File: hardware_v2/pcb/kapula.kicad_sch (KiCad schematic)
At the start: 166 parts, among them J1 Conn_02x10_Odd_Even, J2 Conn_02x10_Odd_Even, J3 U.FL, J4 U.FL, J5 U.FL, J6 U.FL, Q1 AO3401A, Q1 BSS84, Q2 AO3400A, Q3 AO3400A, Q4 AO3400A, Q5 AO3401A, T1 BW21S7511A01TF, T2 BW21S7511A01TF, T3 BW21S7511A01TF, T4 BW21S7511A01TF, U1 TP4054, U2 DW01+G, U3 XC6206P332MR, U4 FM8002A, U5 EFR32FG14P233F256GM48-B, U6 DSB221SDN, U7 XA213-G4J, Y1 32768 Hz

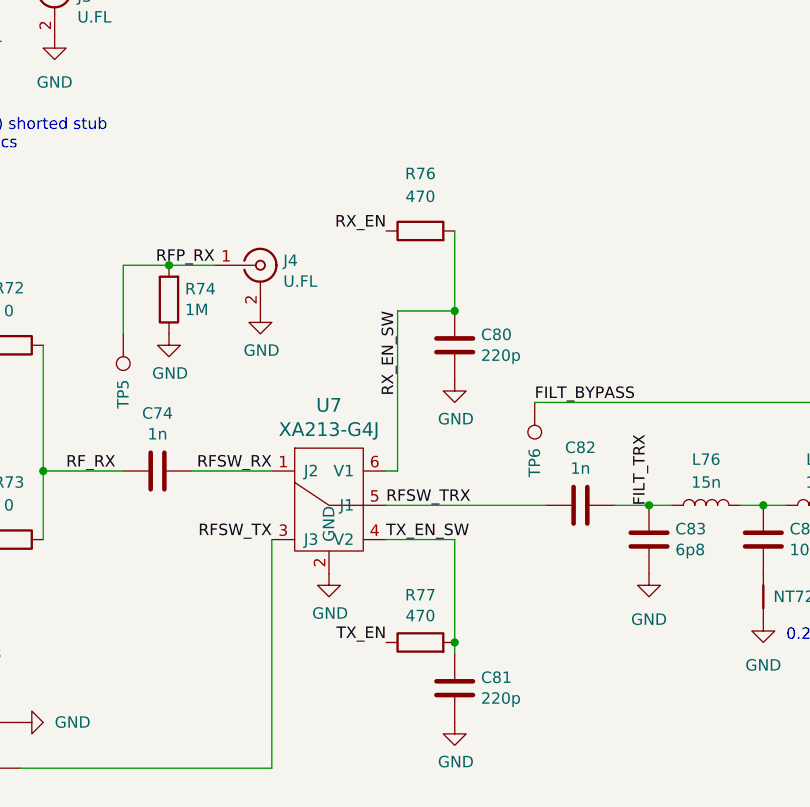
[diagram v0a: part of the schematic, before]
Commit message: PCB: Fix order of RX/TX switch control pins
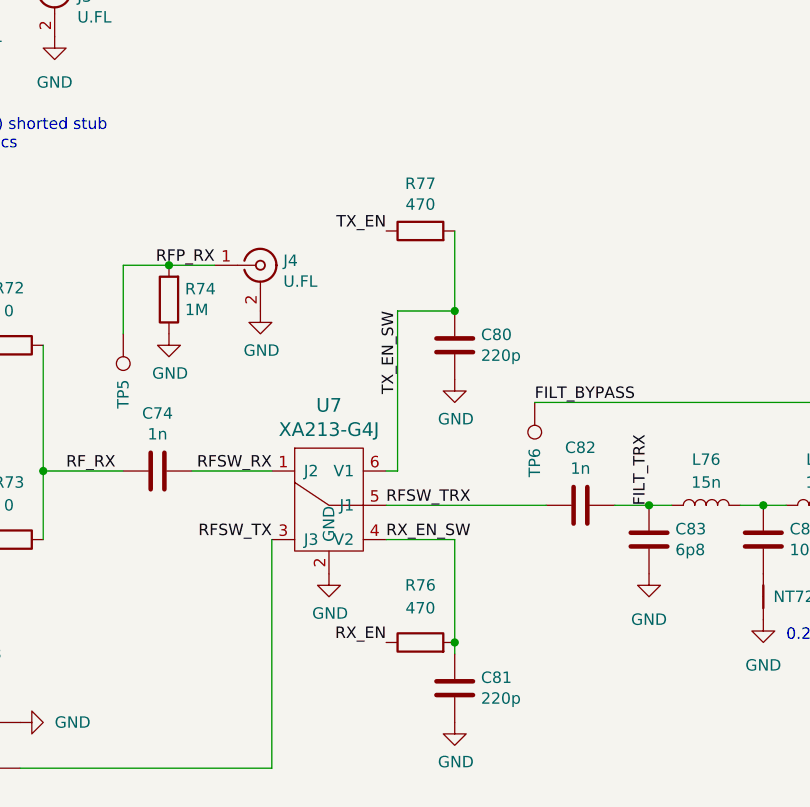
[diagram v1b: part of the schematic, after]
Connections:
- net RX_EN_SW: now also C81.1, U7.4 (V2); no longer C80.1, U7.6 (V1)
- net TX_EN_SW: now also C80.1, U7.6 (V1); no longer C81.1, U7.4 (V2)
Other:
- moved on the sheet: R76, R77
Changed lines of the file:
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@@
   (junction (at 143.51 82.55) (diameter 0) (color 0 0 0 0)
   )
-  (junction (at 283.21 227.33) (diameter 0) (color 0 0 0 0)
-  )
   (junction (at 110.49 238.76) (diameter 0) (color 0 0 0 0)
   )
@@
   (junction (at 200.66 247.65) (diameter 0) (color 0 0 0 0)
   )
+  (junction (at 283.21 227.33) (diameter 0) (color 0 0 0 0)
+  )
   (junction (at 304.8 212.09) (diameter 0) (color 0 0 0 0)
   )
@@
     (stroke (width 0) (type default))
   )
-  (wire (pts (xy 283.21 227.33) (xy 283.21 228.6))
-    (stroke (width 0) (type default))
-  )
   (wire (pts (xy 153.67 82.55) (xy 162.56 82.55))
     (stroke (width 0) (type default))
@@
     (stroke (width 0) (type default))
   )
+  (wire (pts (xy 283.21 227.33) (xy 283.21 228.6))
+    (stroke (width 0) (type default))
+  )
   (wire (pts (xy 53.34 31.75) (xy 44.45 31.75))
     (stroke (width 0) (type default))
@@
     (effects (font (size 1.27 1.27)) (justify left bottom))
   )
-  (label "RX_EN_SW" (at 276.86 190.5 270) (fields_autoplaced)
-    (effects (font (size 1.27 1.27)) (justify right bottom))
+  (label "RX_EN_SW" (at 275.59 215.9 0) (fields_autoplaced)
+    (effects (font (size 1.27 1.27)) (justify left bottom))
   )
   (label "VOL_Out" (at 106.68 102.87 0) (fields_autoplaced)
@@
     (effects (font (size 1.27 1.27)) (justify left bottom))
   )
-  (label "TX_EN_SW" (at 275.59 215.9 0) (fields_autoplaced)
-    (effects (font (size 1.27 1.27)) (justify left bottom))
+  (label "TX_EN_SW" (at 276.86 190.5 270) (fields_autoplaced)
+    (effects (font (size 1.27 1.27)) (justify right bottom))
   )
   (label "D_SDA" (at 364.49 25.4 180) (fields_autoplaced)
@@
     (effects (font (size 1.27 1.27)) (justify right bottom))
   )
-  (label "RX_EN" (at 275.59 181.61 180) (fields_autoplaced)
+  (label "RX_EN" (at 275.59 227.33 180) (fields_autoplaced)
     (effects (font (size 1.27 1.27)) (justify right bottom))
   )
@@
     (effects (font (size 1.27 1.27)) (justify left bottom))
   )
-  (label "TX_EN" (at 275.59 227.33 180) (fields_autoplaced)
+  (label "TX_EN" (at 275.59 181.61 180) (fields_autoplaced)
     (effects (font (size 1.27 1.27)) (justify right bottom))
   )
@@
     )
   )
-  (symbol (lib_id "Device:R") (at 279.4 181.61 90) (unit 1)
+  (symbol (lib_id "Device:R") (at 279.4 227.33 90) (unit 1)
     (in_bom yes) (on_board yes) (dnp no) (fields_autoplaced)
-    (property "Reference" "R76" (at 279.4 175.26 90)
+    (property "Reference" "R76" (at 279.4 220.98 90)
       (effects (font (size 1.27 1.27)))
     )
-    (property "Value" "470" (at 279.4 177.8 90)
+    (property "Value" "470" (at 279.4 223.52 90)
       (effects (font (size 1.27 1.27)))
     )
-    (property "Footprint" "Resistor_SMD:R_0402_1005Metric" (at 279.4 183.388 90)
+    (property "Footprint" "Resistor_SMD:R_0402_1005Metric" (at 279.4 229.108 90)
       (effects (font (size 1.27 1.27)) hide)
     )
-    (property "Datasheet" "" (at 279.4 181.61 0)
+    (property "Datasheet" "" (at 279.4 227.33 0)
       (effects (font (size 1.27 1.27)) hide)
     )
-    (property "LCSC" "C25117" (at 279.4 181.61 0)
+    (property "LCSC" "C25117" (at 279.4 227.33 0)
       (effects (font (size 1.27 1.27)) hide)
     )
@@
     )
   )
-  (symbol (lib_id "Device:R") (at 279.4 227.33 90) (unit 1)
+  (symbol (lib_id "Device:R") (at 279.4 181.61 90) (unit 1)
     (in_bom yes) (on_board yes) (dnp no)
-    (property "Reference" "R77" (at 279.4 222.0722 90)
+    (property "Reference" "R77" (at 279.4 176.3522 90)
       (effects (font (size 1.27 1.27)))
     )
-    (property "Value" "470" (at 279.4 224.3836 90)
+    (property "Value" "470" (at 279.4 178.6636 90)
       (effects (font (size 1.27 1.27)))
     )
-    (property "Footprint" "Resistor_SMD:R_0402_1005Metric" (at 279.4 229.108 90)
+    (property "Footprint" "Resistor_SMD:R_0402_1005Metric" (at 279.4 183.388 90)
       (effects (font (size 1.27 1.27)) hide)
     )
-    (property "Datasheet" "" (at 279.4 227.33 0)
+    (property "Datasheet" "" (at 279.4 181.61 0)
       (effects (font (size 1.27 1.27)) hide)
     )
-    (property "LCSC" "C25117" (at 279.4 227.33 0)
+    (property "LCSC" "C25117" (at 279.4 181.61 0)
       (effects (font (size 1.27 1.27)) hide)
     )

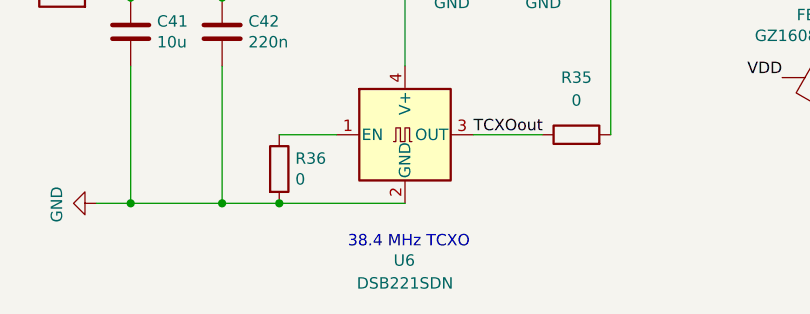
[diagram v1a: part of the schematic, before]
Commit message: PCB: Fix TCXO model in schematic
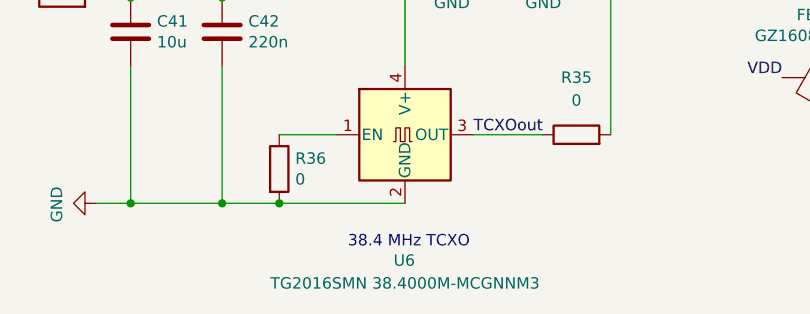
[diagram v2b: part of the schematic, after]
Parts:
- U6: value DSB221SDN -> TG2016SMN 38.4000M-MCGNNM3
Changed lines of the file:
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@@
       (effects (font (size 1.27 1.27)) (justify left))
     )
-    (property "Value" "DSB221SDN" (at 105.41 281.94 0)
+    (property "Value" "TG2016SMN 38.4000M-MCGNNM3" (at 105.41 281.94 0)
       (effects (font (size 1.27 1.27)))
     )

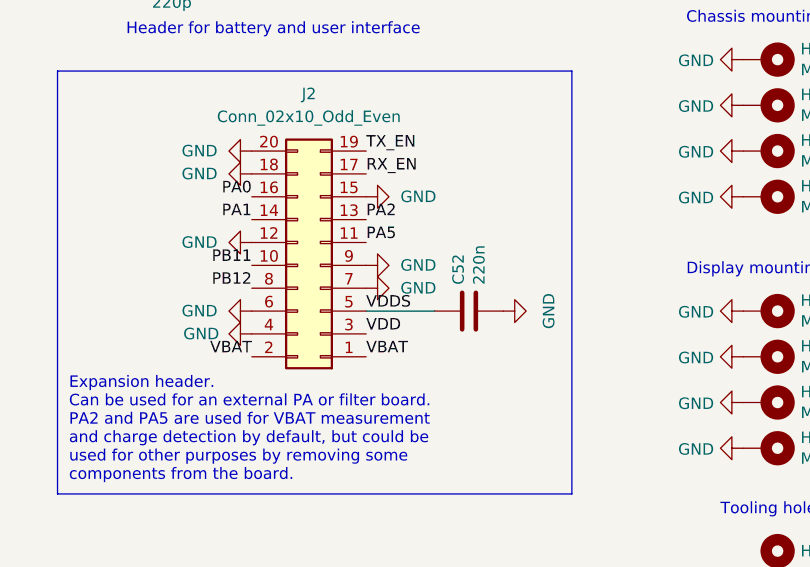
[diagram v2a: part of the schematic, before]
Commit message: PCB: Add DVDD to expansion header
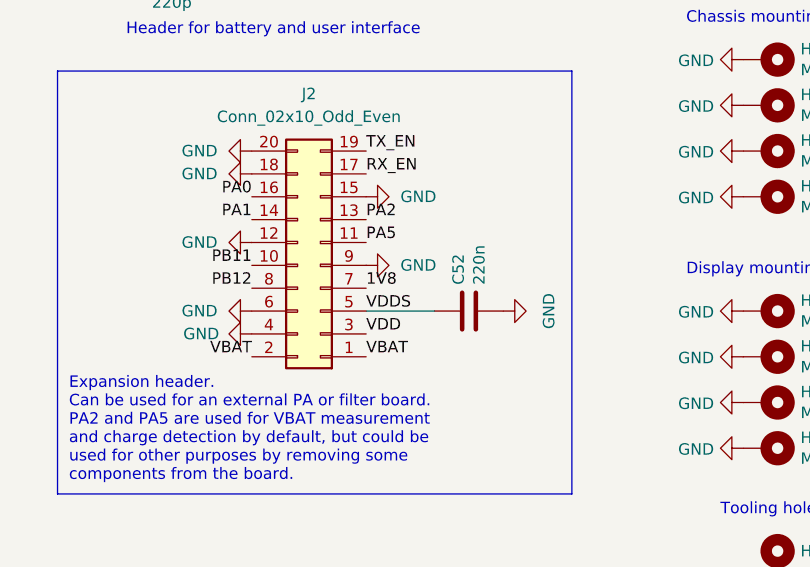
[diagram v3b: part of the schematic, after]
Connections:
- net 1V8: now also J2.7 (Pin_7)
- net GND: no longer J2.7 (Pin_7)
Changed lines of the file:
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@@
     (effects (font (size 1.27 1.27)) (justify right bottom))
   )
+  (label "1V8" (at 344.17 123.19 0) (fields_autoplaced)
+    (effects (font (size 1.27 1.27)) (justify left bottom))
+  )
   (label "VDD" (at 247.65 26.67 0) (fields_autoplaced)
     (effects (font (size 1.27 1.27)) (justify left bottom))
@@
         )
       )
-    )
-  )
-  (symbol (lib_id "power:GND") (at 344.17 123.19 90) (unit 1)
-    (in_bom yes) (on_board yes) (dnp no) (fields_autoplaced)
-    (property "Reference" "#PWR0101" (at 350.52 123.19 0)
-      (effects (font (size 1.27 1.27)) hide)
-    )
-    (property "Value" "GND" (at 347.98 123.19 90)
-      (effects (font (size 1.27 1.27)) (justify right))
-    )
-    (property "Footprint" "" (at 344.17 123.19 0)
-      (effects (font (size 1.27 1.27)) hide)
-    )
-    (property "Datasheet" "" (at 344.17 123.19 0)
-      (effects (font (size 1.27 1.27)) hide)
-    )
-    (pin "1")
-    (instances
-      (project "kapula"
-        (path "/f2315993-072e-45c9-8c85-e79c6d40aba4"
-          (reference "#PWR0101") (unit 1)
-        )
-      )

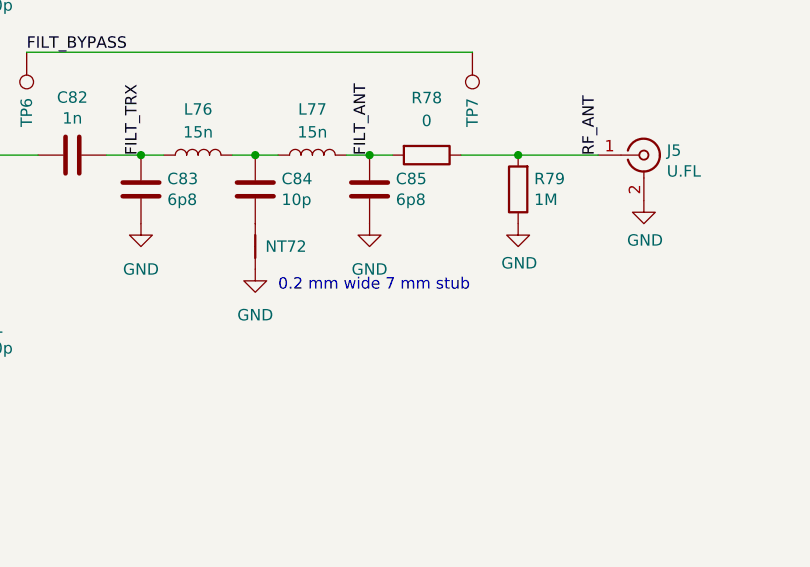
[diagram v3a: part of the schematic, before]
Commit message: PCB: Optimize lowpass filter
* Reduce second harmonic stub length by 1 mm
  to move notch frequency closer to 870 MHz.
* Use footprints of correct size for capacitors and inductors.
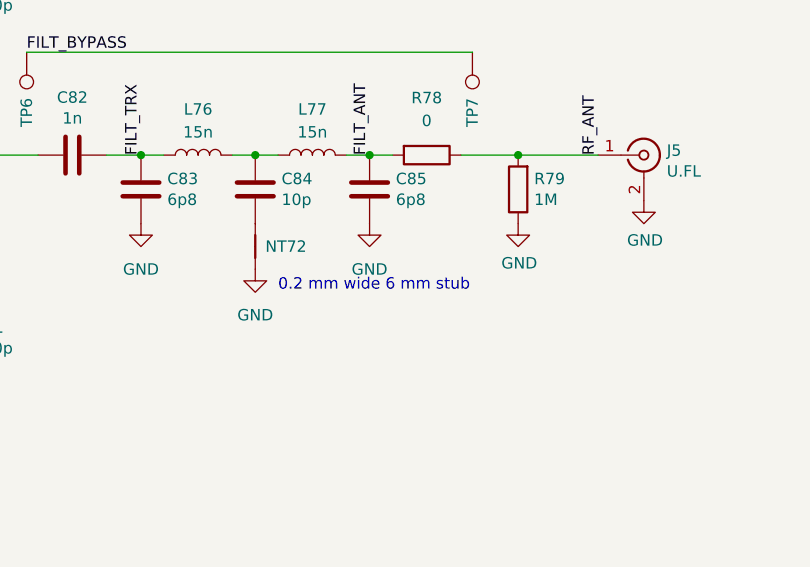
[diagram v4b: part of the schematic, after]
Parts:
- C83, C84, C85: footprint kapula:C_0402_to_0603_HandSolder -> Capacitor_SMD:C_0603_1608Metric_Pad1.08x0.95mm_HandSolder
- L76, L77: footprint kapula:L_0402_to_0603_HandSolder -> Inductor_SMD:L_0402_1005Metric_Pad0.77x0.64mm_HandSolder
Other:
- note added: "0.2 mm wide 6 mm stub"
- note removed: "0.2 mm wide 7 mm stub"
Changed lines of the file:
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@@
     (effects (font (size 1.27 1.27)) (justify left bottom))
   )
-  (text "0.2 mm wide 7 mm stub" (at 320.04 227.33 0)
+  (text "0.2 mm wide 6 mm stub" (at 320.04 227.33 0)
     (effects (font (size 1.27 1.27)) (justify left bottom))
   )
@@
       (effects (font (size 1.27 1.27)) (justify left))
     )
-    (property "Footprint" "kapula:C_0402_to_0603_HandSolder" (at 318.4652 219.71 0)
+    (property "Footprint" "Capacitor_SMD:C_0603_1608Metric_Pad1.08x0.95mm_HandSolder" (at 318.4652 219.71 0)
       (effects (font (size 1.27 1.27)) hide)
     )
@@
       (effects (font (size 1.27 1.27)))
     )
-    (property "Footprint" "kapula:L_0402_to_0603_HandSolder" (at 323.85 212.09 0)
+    (property "Footprint" "Inductor_SMD:L_0402_1005Metric_Pad0.77x0.64mm_HandSolder" (at 323.85 212.09 0)
       (effects (font (size 1.27 1.27)) hide)
     )
@@
       (effects (font (size 1.27 1.27)) (justify left))
     )
-    (property "Footprint" "kapula:C_0402_to_0603_HandSolder" (at 331.1652 219.71 0)
+    (property "Footprint" "Capacitor_SMD:C_0603_1608Metric_Pad1.08x0.95mm_HandSolder" (at 331.1652 219.71 0)
       (effects (font (size 1.27 1.27)) hide)
     )
@@
       (effects (font (size 1.27 1.27)))
     )
-    (property "Footprint" "kapula:L_0402_to_0603_HandSolder" (at 311.15 212.09 0)
+    (property "Footprint" "Inductor_SMD:L_0402_1005Metric_Pad0.77x0.64mm_HandSolder" (at 311.15 212.09 0)
       (effects (font (size 1.27 1.27)) hide)
     )
@@
       (effects (font (size 1.27 1.27)) (justify left))
     )
-    (property "Footprint" "kapula:C_0402_to_0603_HandSolder" (at 305.7652 219.71 0)
+    (property "Footprint" "Capacitor_SMD:C_0603_1608Metric_Pad1.08x0.95mm_HandSolder" (at 305.7652 219.71 0)
       (effects (font (size 1.27 1.27)) hide)
     )

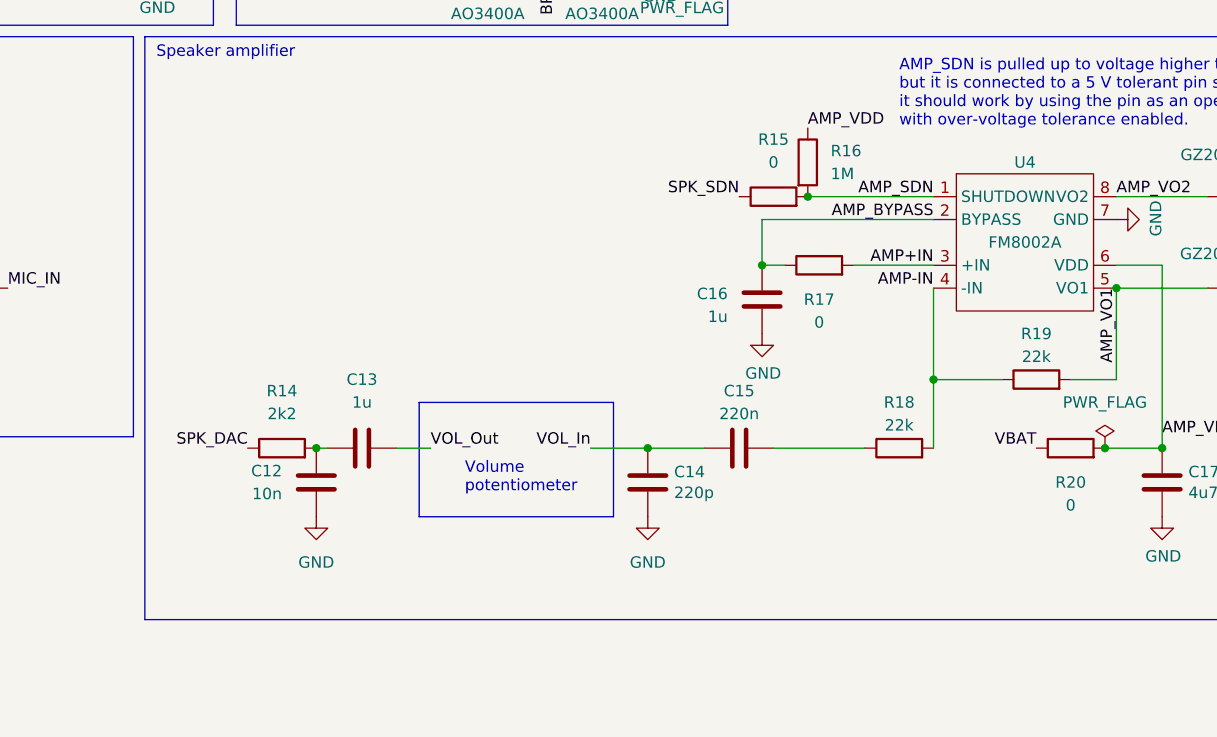
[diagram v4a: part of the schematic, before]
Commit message: PCB: Changes to audio power amplifier circuit
* Increase maximum gain
* Change some footprint sizes
* Reduce shutdown pull-up resistor value
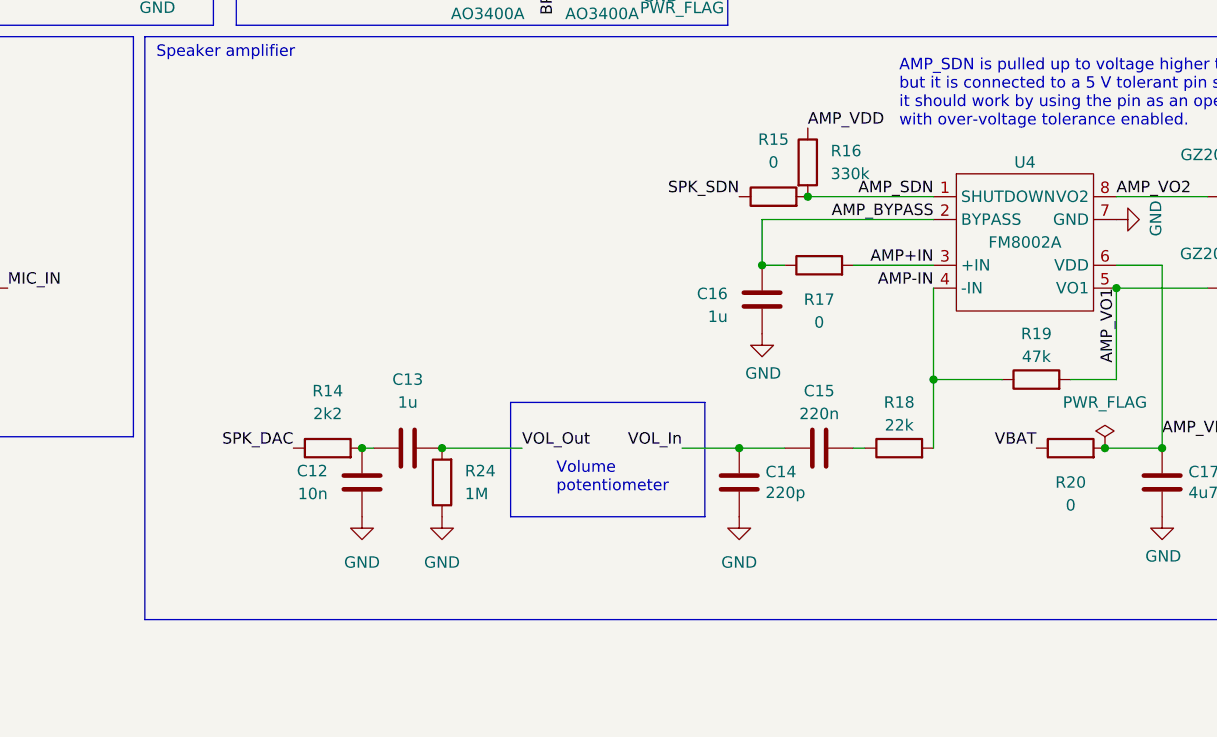
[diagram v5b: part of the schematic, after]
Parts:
- added R24: 1M, Resistor_SMD:R_0402_1005Metric, symbol Device:R
- C15: footprint kapula:C_0402_to_0603_HandSolder -> Capacitor_SMD:C_0402_1005Metric_Pad0.74x0.62mm_HandSolder
- R16: value 1M -> 330k; LCSC C26083 -> C25778
- R18: footprint Resistor_SMD:R_0402_1005Metric -> Resistor_SMD:R_0603_1608Metric_Pad0.98x0.95mm_HandSolder; LCSC C25768 -> C31850
- R19: value 22k -> 47k; footprint Resistor_SMD:R_0402_1005Metric -> Resistor_SMD:R_0603_1608Metric_Pad0.98x0.95mm_HandSolder; LCSC C25768 -> C25819
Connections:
- net GND: now also R24.1
- net VOL_Out: now also R24.2
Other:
- moved on the sheet: C12, C13, C14, C15, R14

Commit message: PCB: Improve battery charger cooling by adding zones for all pins
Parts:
- R2: footprint kapula:R_0402_to_0603_HandSolder -> Resistor_SMD:R_0603_1608Metric_Pad0.98x0.95mm_HandSolder
- R4: footprint kapula:R_0402_to_0603_HandSolder -> Resistor_SMD:R_0603_1608Metric
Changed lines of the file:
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@@
       (effects (font (size 1.27 1.27)) (justify left))
     )
-    (property "Footprint" "kapula:R_0402_to_0603_HandSolder" (at 74.422 45.72 90)
+    (property "Footprint" "Resistor_SMD:R_0603_1608Metric_Pad0.98x0.95mm_HandSolder" (at 74.422 45.72 90)
       (effects (font (size 1.27 1.27)) hide)
     )
@@
       (effects (font (size 1.27 1.27)) (justify left))
     )
-    (property "Footprint" "kapula:R_0402_to_0603_HandSolder" (at 130.302 43.18 90)
-      (effects (font (size 1.27 1.27)) hide)
-    )
+    (property "Footprint" "Resistor_SMD:R_0603_1608Metric" (at 130.302 43.18 90)
+      (effects (font (size 1.27 1.27)) hide)
+    )
